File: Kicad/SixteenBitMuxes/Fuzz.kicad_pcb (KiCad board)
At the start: 2 copper layers, 100 x 82 mm, 104 parts, among them J1 Audio In/Out JST XH, J10 JST XH Buttons, J11 LCD JST XH, J12 Bypass Switch JST XH, J2 TONE_POTS, J4 VOL POT A100K JST XH, J5 PowerTest_PinHeader, J6 9V Power JST XH, J7 Boot Reset PinHeader, J9 SWD_PinHeader, Q1 PN2222A, Q10 2SC1815, Q11 PN2222A, Q12 S9013, Q13 MMBT3904, Q14 S9018, Q15 BC848B, Q16 2SC1623, Q17 MPSA18, Q18 MMBT5551L, Q19 2N5088, Q2 MMBT3904, Q20 MMBTA42, Q21 BC807, Q22 BC846, Q23 BC847B, Q24 BC847C, Q25 BC848B, Q26 S9013, Q27 S9018, Q28 C945, Q29 2SC1623, Q3 MMBT5551L, Q30 2SC1815, Q31 MPSA18, Q32 2N5088, Q4 MMBTA42, Q5 BC807, Q6 BC846, Q7 BC847B, Q8 BC847C, Q9 C945, U1 AMS1117-5.0, U2 AMS1117-3.3, U21 CD4051B, U22 4504, U23 4504, U24 4504, U25 CD4053B, U3 STM32F103C8Tx, U4 CD4051B, U6 CD4067BM, U7 CD4067BM, U8 CD4067BM, U9 CD4067BM, Y1 8MHz

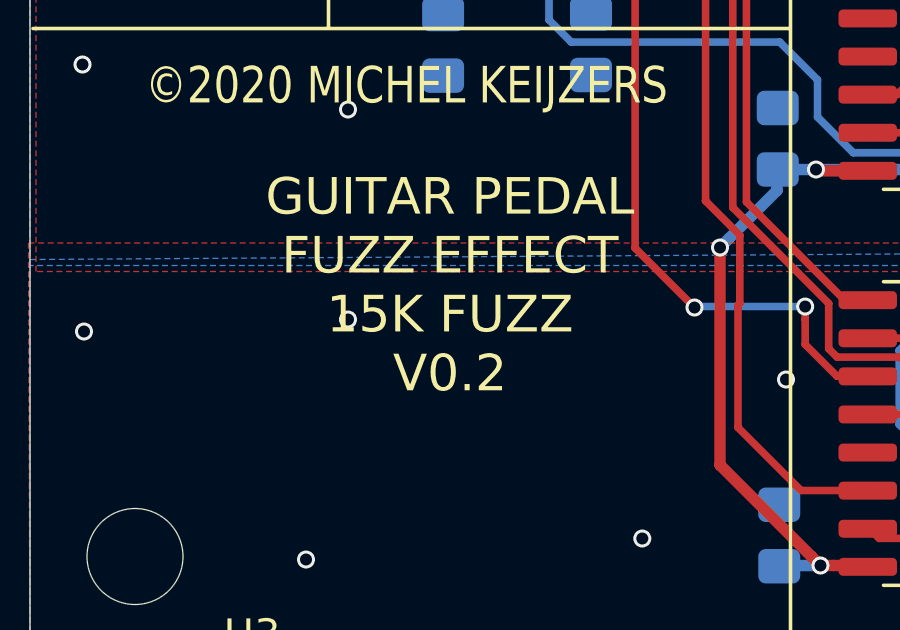
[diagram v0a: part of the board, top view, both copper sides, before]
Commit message: 25K->16K Fuzz
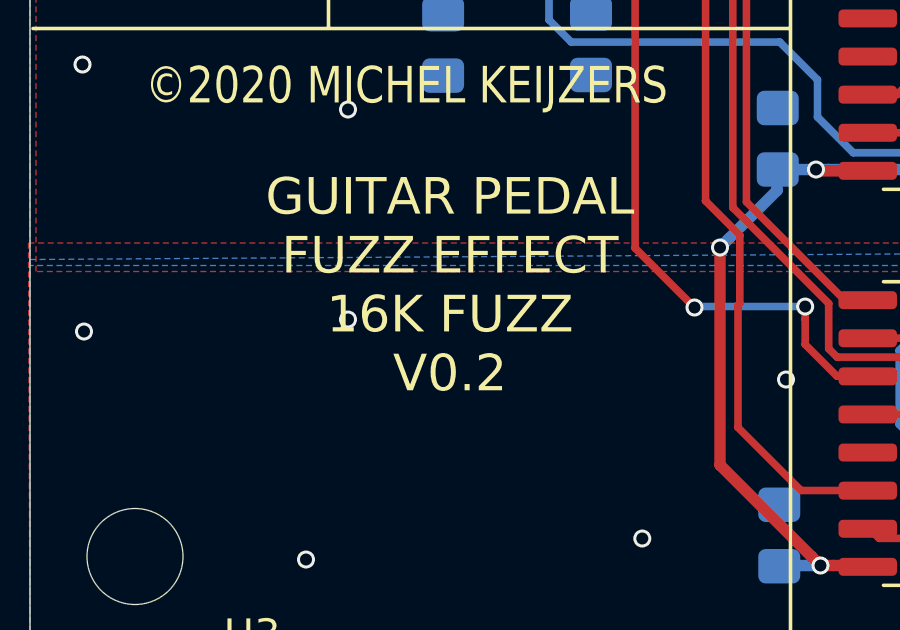
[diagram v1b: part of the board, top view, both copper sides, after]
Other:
- board text added: "GUITAR PEDAL FUZZ EFFECT 16K FUZZ V0.2"
- board text removed: "GUITAR PEDAL FUZZ EFFECT 15K FUZZ V0.2"
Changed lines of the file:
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@@
     (effects (font (size 1.016 0.8128) (thickness 0.1524)))
   )
-  (gr_text "GUITAR PEDAL \nFUZZ EFFECT\n15K FUZZ\nV0.2" (at 44 99.45) (layer F.SilkS)
+  (gr_text "GUITAR PEDAL \nFUZZ EFFECT\n16K FUZZ\nV0.2" (at 44 99.45) (layer F.SilkS)
     (effects (font (size 1.2192 1.2192) (thickness 0.254)))
   )

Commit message: Improvements according video youtube
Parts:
- added C20: 10uF, Capacitor_SMD:C_0805_2012Metric_Pad1.15x1.40mm_HandSolder, B.Cu at (52.8, 64.5)
- added F1: 1.1A(1812), Inductor_SMD:L_1812_4532Metric_Pad1.30x3.40mm_HandSolder, B.Cu at (49.5, 50.7)
- added FB1: 1K/100MHz, Inductor_SMD:L_0805_2012Metric_Pad1.15x1.40mm_HandSolder, B.Cu at (49.2, 58.0)
- added R5: 220R, Resistor_SMD:R_0805_2012Metric_Pad1.15x1.40mm_HandSolder, B.Cu at (54.5, 81.7)
- added R6: 10K, Resistor_SMD:R_0805_2012Metric_Pad1.15x1.40mm_HandSolder, B.Cu at (40.9, 74.2)
- added R7: 10K, Resistor_SMD:R_0805_2012Metric_Pad1.15x1.40mm_HandSolder, B.Cu at (37.2, 74.2)
- added REF**: KiCad-Logo_6mm_SilkScreen, Symbol:KiCad-Logo_6mm_SilkScreen, F.Cu at (46.0, 105.8)
- H1, H2, H3, H4: value MountingHole -> MountingHole_Pad; footprint MountingHole:MountingHole_3.2mm_M3 -> MountingHole:MountingHole_3mm_Pad_Via
- J9: value SWD_PinHeader -> SWD PinHeader; footprint Connector_PinHeader_2.54mm:PinHeader_1x04_P2.54mm_Vertical -> Connector_PinHeader_2.54mm:PinHeader_1x05_P2.54mm_Vertical
- RN2: value R_Pack04 -> 33R
- U21, U4: value CD4051B -> CD4051BM
- U22, U23, U24: value 4504 -> CD4504BM
- U25: value CD4053B -> CD4053BM
- U3: value STM32F103C8Tx -> STM32F103C8T6
- Y1: footprint Crystal:Crystal_HC49-U_Vertical -> Crystal:Crystal_HC49-4H_Vertical
- moved H1 92.4 mm to (34.1, 34.1)
- moved H3 92.4 mm to (125.8, 107.8)
- moved H2 74.5 mm to (125.9, 34.0)
- moved H4 74.4 mm to (34.1, 107.8)
- moved R4 6.43 mm to (52.8, 58.0)
- moved J9 3.16 mm to (33.6, 65.4)
- moved C3 1.81 mm to (41.2, 43.7), turned to 270 degrees
- moved Q18 0.60 mm to (114.8, 90.0)
- moved Q13 0.25 mm to (104.2, 90.0)
- turned D2 to 90 degrees
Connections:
- net /Mcu/PB2 renamed /Mcu/BOOT1
- net Net-(C5-Pad1) renamed /Mcu/OSC_IN
- C11 pad 1: +9V -> /+9V_SAFE
- C2 pad 1: Net-(C2-Pad1) -> /+9V_SAFE
- C21 pad 1: +9V -> /+9V_SAFE
- C22 pad 1: +9V -> /+9V_SAFE
- C23 pad 1: +9V -> /+9V_SAFE
- C24 pad 1: +9V -> /+9V_SAFE
- C36 pad 1: +9V -> /+9V_SAFE
- C45 pad 1: +9V -> /+9V_SAFE
- C46 pad 1: +9V -> /+9V_SAFE
- C47 pad 1: +9V -> /+9V_SAFE
- C48 pad 1: +9V -> /+9V_SAFE
- D2 pad 1: Net-(C2-Pad1) -> Net-(D2-Pad1)
- H1 pad 1: (no net) -> GND
- H2 pad 1: (no net) -> GNDA
- H3 pad 1: (no net) -> GNDA
- H4 pad 1: (no net) -> GND
- R1 pad 1: +9V -> /+9V_SAFE
- R3 pad 1: +9V -> /+9V_SAFE
- R4 pad 1: +9V -> /+9V_SAFE
- U1 pad 3: Net-(C2-Pad1) -> /+9V_SAFE
- U2 pad 3: Net-(C2-Pad1) -> /+9V_SAFE
- U21 pad 16: +9V -> /+9V_SAFE
- U22 pad 16: +9V -> /+9V_SAFE
- U23 pad 16: +9V -> /+9V_SAFE
- U24 pad 16: +9V -> /+9V_SAFE
- U25 pad 16: +9V -> /+9V_SAFE
- U3 pad 1: Net-(U3-Pad1) -> +3V3
- U3 pad 38: Net-(U3-Pad38) -> /Mcu/GPIO_BUTTON_DECREASE
- U3 pad 39: /Mcu/GPIO_BUTTON_DECREASE -> /Mcu/SYS_JTDO_TRACESWO
- U3 pad 44: GND -> Net-(R6-Pad1)
- U3 pad 6: Net-(C6-Pad1) -> /Mcu/OSC_OUT
- U3 pad 8: Net-(U3-Pad8) -> +3V3
- U4 pad 16: +9V -> /+9V_SAFE
- U6 pad 24: +9V -> /+9V_SAFE
- U7 pad 24: +9V -> /+9V_SAFE
- U8 pad 24: +9V -> /+9V_SAFE
- U9 pad 24: +9V -> /+9V_SAFE
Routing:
- net /+9V_SAFE: track 0.00 -> 268.7 mm, vias 0 -> 14
- net +9V: track 279.5 -> 29.6 mm, vias 15 -> 0
- net Net-(C2-Pad1): track 27.9 -> 0.00 mm, vias 1 -> 0
- net /Mcu/SYS_JTDO_TRACESWO: track 0.00 -> 18.3 mm, vias 0 -> 1
- net +5V: track 76.9 -> 64.7 mm
- net +3V3: track 179.1 -> 189.1 mm
- net GND: track 91.2 -> 100.8 mm, vias 55 -> 56
- net Net-(R6-Pad1): track 0.00 -> 7.84 mm, vias 0 -> 1
- net /Mcu/OSC_OUT: track 0.00 -> 6.42 mm, vias 0 -> 1
- net Net-(D1-Pad2): track 9.12 -> 3.62 mm
- net Net-(D2-Pad1): track 0.00 -> 5.45 mm
- net Net-(C6-Pad1): track 17.5 -> 12.9 mm, vias 1 -> 0
- net Net-(F1-Pad2): track 0.00 -> 4.17 mm
- net /Mcu/BOOT1: track 33.7 -> 37.5 mm
- net /Mcu/SYS_JTMS_SWDIO: track 17.4 -> 14.3 mm
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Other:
- outline, holes or cut-outs redrawn
- board text added: "5V GND CLK DIO SWO"
- board text removed: "5V GND CLK DIO"
- board text removed: "VOLTAGE REGULATOR DIODES"

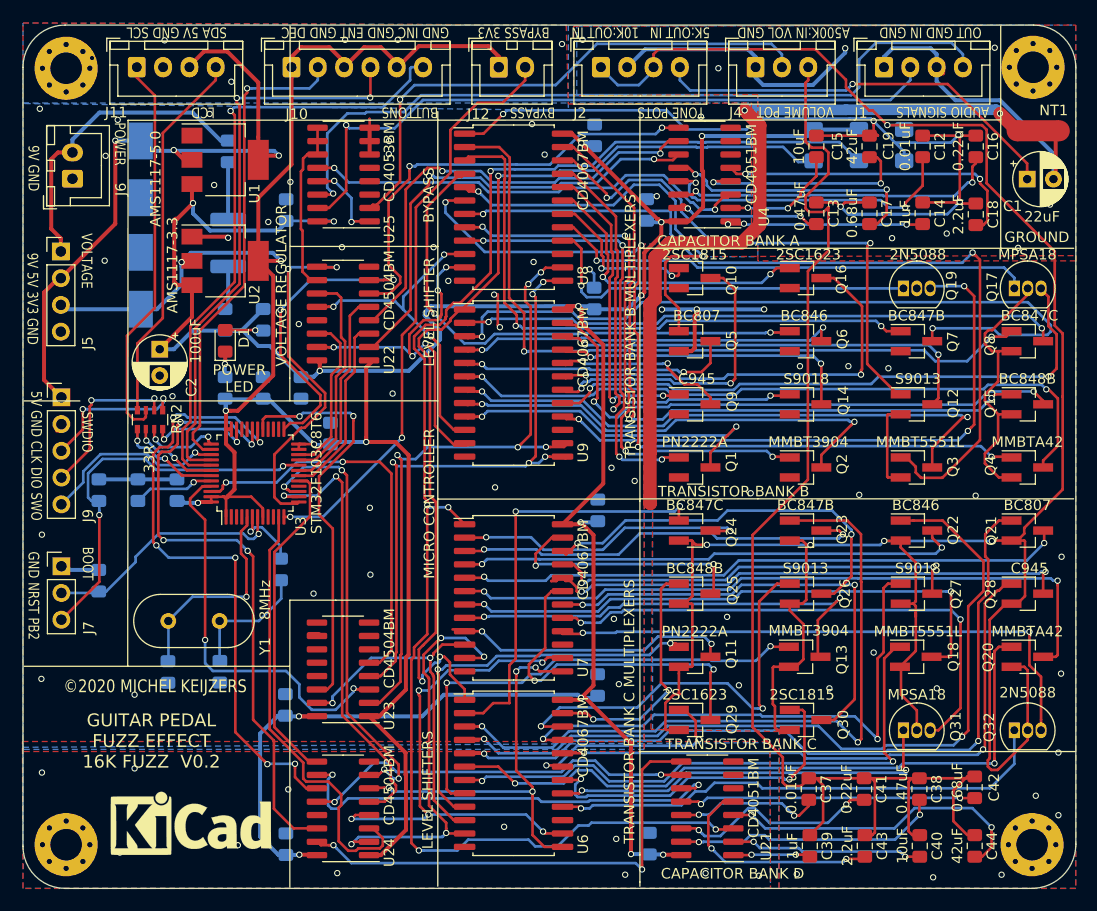
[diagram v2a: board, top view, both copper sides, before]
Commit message: UART, BOOT, NRST, Isolated OSC gnd
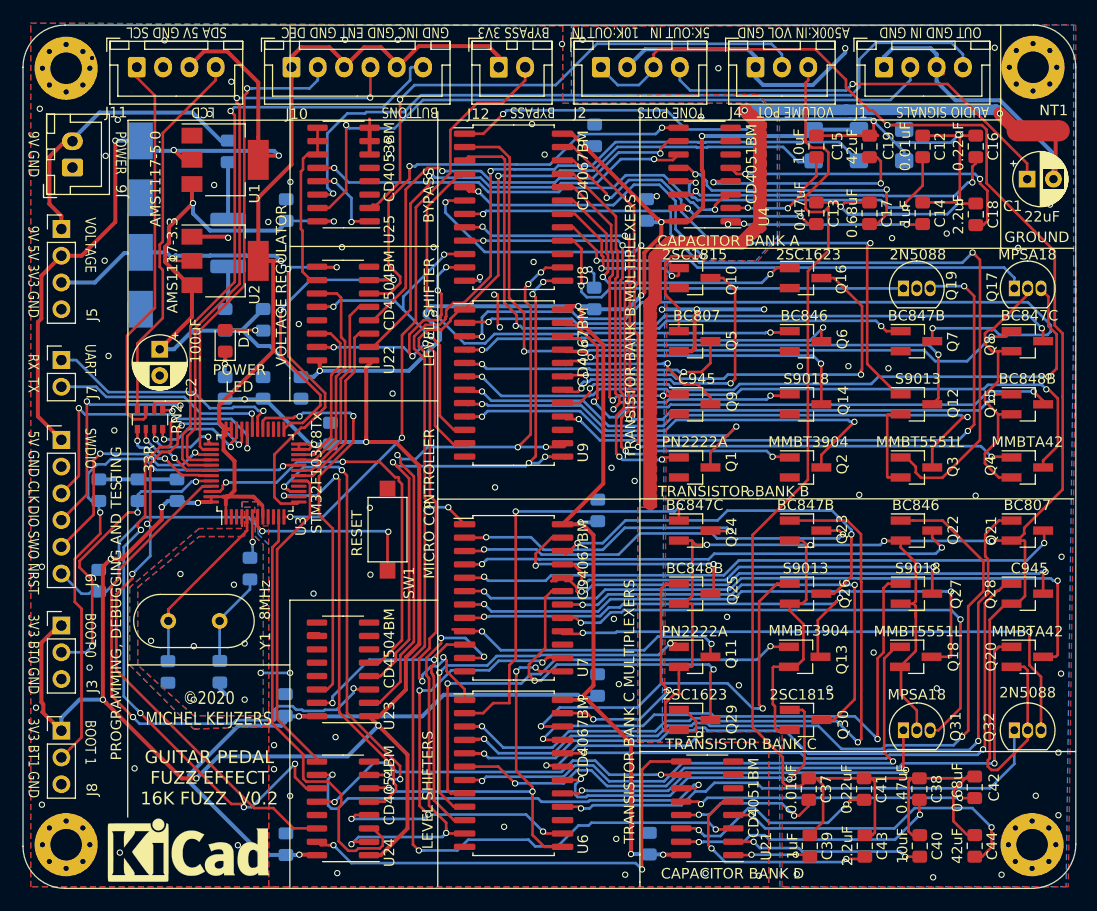
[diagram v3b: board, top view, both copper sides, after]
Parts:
- added J3: Jumper BOOT0, Connector_PinHeader_2.54mm:PinHeader_1x03_P2.54mm_Vertical, F.Cu at (33.6, 87.0)
- added J8: Jumper BOOT1, Connector_PinHeader_2.54mm:PinHeader_1x03_P2.54mm_Vertical, F.Cu at (33.6, 97.0)
- added SW1: RESET, Button_Switch_SMD:SW_SPST_CK_RS282G05A3, F.Cu at (64.6, 77.9)
- F1: value 1.1A(1812) -> Polyfuse 1.1A (1812)
- FB1: value 1K/100MHz -> 1K, 100MHz
- J7: value Boot Reset PinHeader -> UART Pin Header; footprint Connector_PinHeader_2.54mm:PinHeader_1x03_P2.54mm_Vertical -> Connector_PinHeader_2.54mm:PinHeader_1x02_P2.54mm_Vertical
- J9: value SWD PinHeader -> SWD; footprint Connector_PinHeader_2.54mm:PinHeader_1x05_P2.54mm_Vertical -> Connector_PinHeader_2.54mm:PinHeader_1x06_P2.54mm_Vertical
- U24: value CD4504BM -> CD4054BM
- U3: value STM32F103C8T6 -> STM32F103C8Tx
- moved J7 19.6 mm to (33.6, 61.8)
- moved J9 4.04 mm to (33.6, 69.4)
- moved R5 2.91 mm to (51.6, 81.6)
- moved REF** 2.56 mm to (45.7, 108.3)
- moved J5 2.13 mm to (33.6, 49.4)
- moved J6 1.07 mm to (34.7, 43.5)
- turned C4 to 270 degrees
- turned R6 to 270 degrees
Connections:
- J7 pad 1: GND -> /Mcu/UART_RX
- J7 pad 2: /Mcu/NRST -> /Mcu/UART_TX
- R6 pad 1: Net-(R6-Pad1) -> GND
- R6 pad 2: GND -> /Mcu/BOOT0
- U3 pad 30: /CAPACITOR_D_SELECTION_1_3V3 -> /Mcu/UART_RX
- U3 pad 31: /CAPACITOR_D_SELECTION_2_3V3 -> /Mcu/UART_TX
- U3 pad 32: Net-(U3-Pad32) -> /CAPACITOR_D_SELECTION_1_3V3
- U3 pad 33: Net-(U3-Pad33) -> /CAPACITOR_D_SELECTION_2_3V3
- U3 pad 44: Net-(R6-Pad1) -> /Mcu/BOOT0
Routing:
- net +3V3: track 189.1 -> 262.3 mm, vias 6 -> 11
- net /Mcu/BOOT0: track 0.00 -> 28.5 mm, vias 0 -> 3
- net /Mcu/UART_RX: track 0.00 -> 23.3 mm, vias 0 -> 1
- net /Mcu/UART_TX: track 0.00 -> 21.0 mm, vias 0 -> 1
- net /Mcu/NRST: track 23.4 -> 43.1 mm, vias 1 -> 2
- net /TRANSISTOR_B_SELECTION_2_3V3: track 37.9 -> 52.5 mm
- net /Mcu/BOOT1: track 37.5 -> 51.2 mm
- net /Mcu/SYS_JTICK_SWCLK: track 15.7 -> 24.6 mm
- net /+9V_SAFE: track 268.7 -> 277.2 mm
- net Net-(R6-Pad1): track 7.84 -> 0.00 mm, vias 1 -> 0
- net /CAPACITOR_D_SELECTION_1_3V3: track 59.6 -> 65.8 mm
- net +5V: track 64.7 -> 70.1 mm
- net /Mcu/SYS_JTMS_SWDIO: track 14.3 -> 19.0 mm
- net /Mcu/SYS_JTDO_TRACESWO: track 18.3 -> 22.4 mm, vias 1 -> 2
- net Net-(C6-Pad1): track 12.9 -> 9.59 mm
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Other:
- board text added: "3V3 BT0 GND"
- board text added: "3V3 BT1 GND"
- board text added: "5V GND CLK"
- board text added: "BOOT 0"
- board text added: "BOOT 1"
- board text added: "DIO SWO NRST"
- board text added: "PROGRAMMING, DEBUGGING AND TESTING"
- board text added: "RX TX"
- board text added: "UART"
- board text removed: "5V GND CLK DIO SWO"
- board text removed: "BOOT"
- board text removed: "GND NRST PB2"

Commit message: Thicker I2C trace
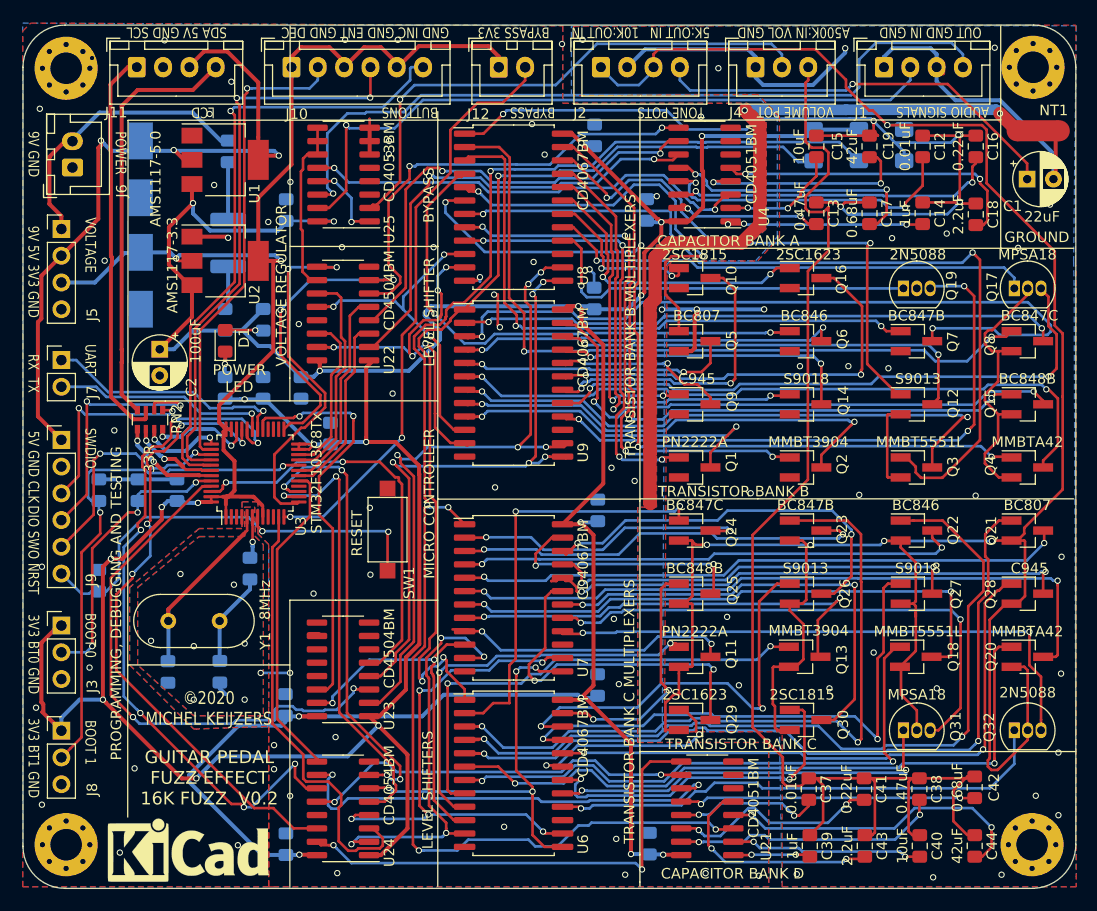
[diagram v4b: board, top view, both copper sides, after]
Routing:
- net /Mcu/I2C1_SDA: track 35.9 -> 40.0 mm
- net /Mcu/BOOT1: track 51.2 -> 50.1 mm
- net /CAPACITOR_D_SELECTION_1_3V3: track 65.8 -> 66.9 mm
- net /Mcu/BOOT0: track 28.5 -> 27.5 mm
- net /Mcu/I2C1_SCL: track 37.4 -> 37.9 mm
- net GND: vias 70 -> 67

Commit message: Various
Various
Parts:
- F1: value Polyfuse 1.1A (1812) -> Polyfuse 1.1A
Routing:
- net /+9V_SAFE: track 276.9 -> 367.4 mm, vias 14 -> 18
- net GND: track 103.0 -> 134.5 mm, vias 67 -> 68
- net +5V: track 69.7 -> 76.0 mm
- net /TRANSISTOR_C_SELECTION_0_3V3: track 38.9 -> 44.9 mm, vias 2 -> 5
- net GNDA: track 107.2 -> 113.2 mm, vias 30 -> 33
- net /TransistorsB/1_BASE: track 41.8 -> 47.3 mm
- net /CAPACITOR_A_SELECTION_2_3V3: track 28.9 -> 23.8 mm
- net Net-(C18-Pad2): track 29.7 -> 34.5 mm
- net /TransistorsB/9_BASE: track 67.1 -> 71.8 mm
- net /TransistorsB/2_BASE: track 53.1 -> 57.0 mm
- net /TRANSISTOR_B_SELECTION_3_3V3: track 39.3 -> 35.7 mm
- net /Mcu/BOOT0: track 27.5 -> 31.1 mm
- net Net-(D1-Pad2): track 3.62 -> 7.13 mm
- net /TransistorsC/16_COLLECTOR: track 54.6 -> 58.1 mm
- net /Mcu/SYS_JTMS_SWDIO: track 19.0 -> 22.2 mm
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
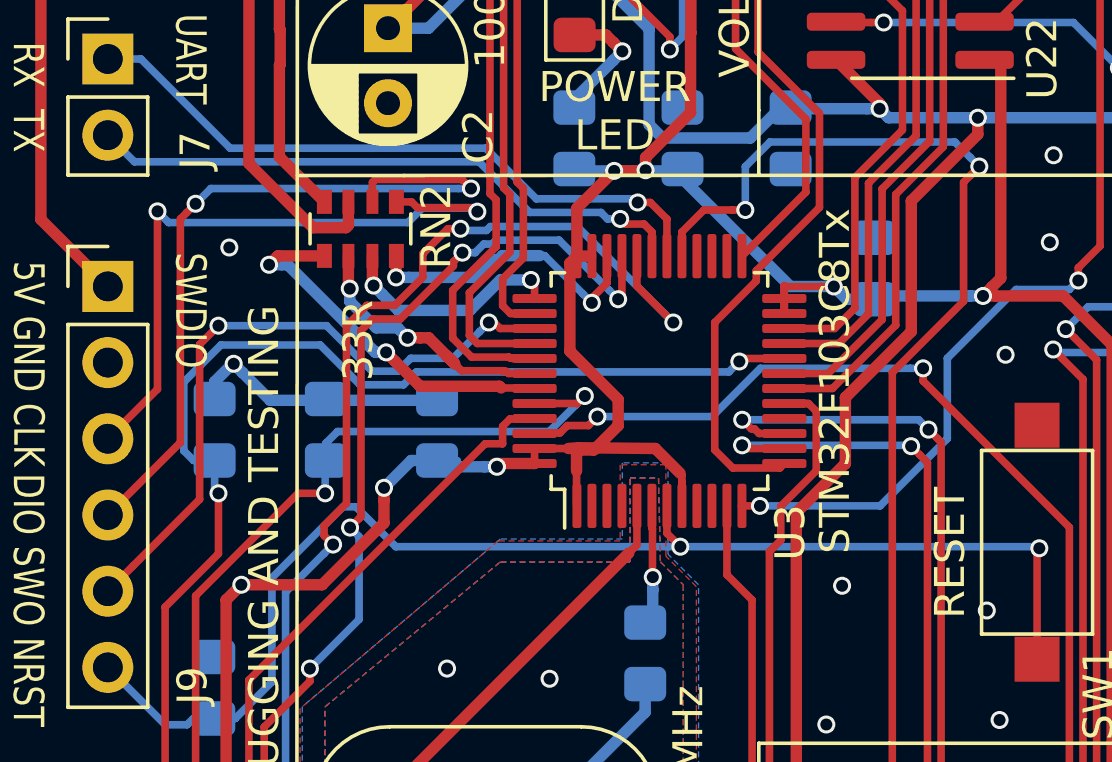
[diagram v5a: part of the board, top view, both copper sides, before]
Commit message: STM32 DevBoard in Freecad
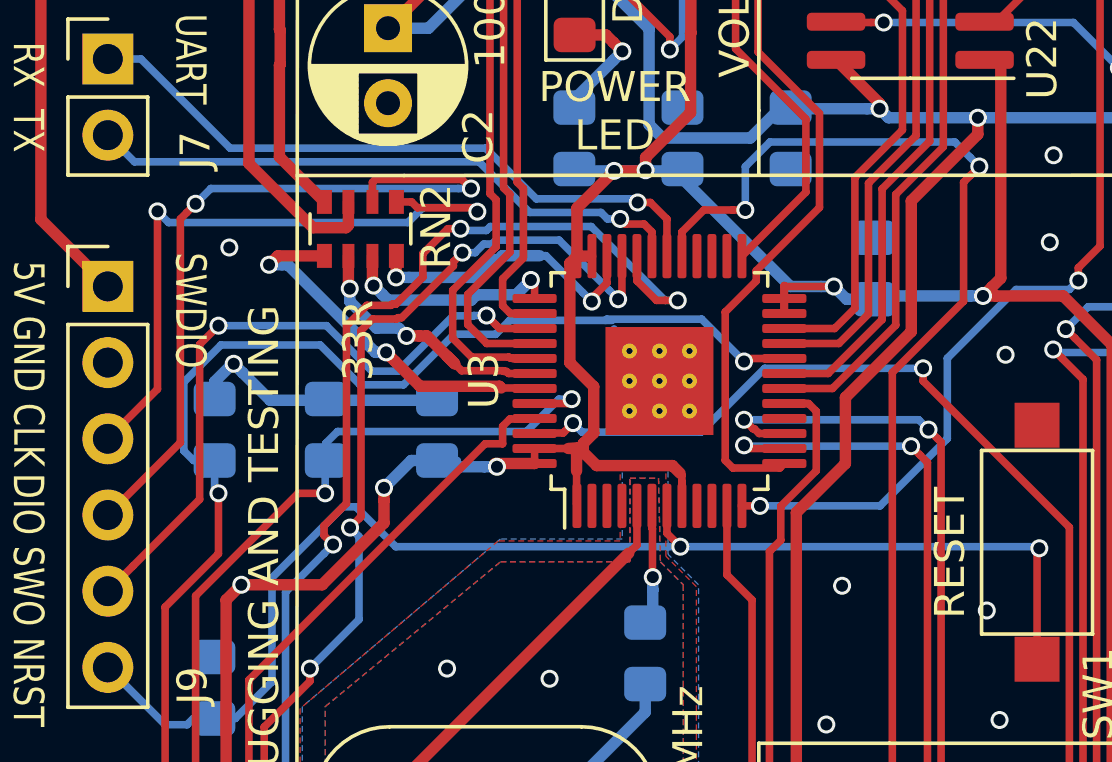
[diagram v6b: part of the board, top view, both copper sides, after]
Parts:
- F1: value Polyfuse 1.1A -> Polyfuse 1.1A (1812L)
- U3: footprint Package_QFP:LQFP-48_7x7mm_P0.5mm -> Package_QFP:LQFP-48-1EP_7x7mm_P0.5mm_EP3.6x3.6mm_ThermalVias
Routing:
- net /Mcu/BOOT1: track 50.9 -> 52.5 mm
- net /Mcu/BOOT0: track 31.1 -> 30.1 mm
- net +3V3: track 263.2 -> 262.3 mm
